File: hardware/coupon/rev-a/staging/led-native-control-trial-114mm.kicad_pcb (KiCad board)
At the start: 6 copper layers, 114 x 32.5 mm, 483 parts, among them J1 USB4505-03-0-A, J2 S2B-PH-SM4-TB, SW1 EVQP7J01P, SW2 JS202011JCQN, U1 TLC59581RTQT, U11 SN74LVC1G04DBVR, U17 SN74LVC1G11DBVR, U2 74HC4514PW,118, U23 SN74LVC1G06DBVR, U24 SN74LVC2G17DBVR, U25 SN74LVC2G17DBVR, U29 TPS70933DBVR, U3 ESP32-S3-WROOM-1U-N16R8, U31 TUSB320LAIRWBR, U32 TS3USB31ERSER, U33 TPD4E05U06DQAR, U34 TPS3808G01DBVR, U35 MAX17048G+T10, U36 TPS631000DRLR, U37 TPS63020DSJT, U38 2.5V shunt, U39 TMP390A2DRLR, U40 SN74AUP1G125DBVR, U41 BQ24074RGTR, U42 SN74AUP1G125DBVR, U43 SN74AUP1G125DBVR, U44 TPS259474ARPWR, U45 TPS259474ARPWR, U46 TCA9517ADGKR, U47 TPS3823A-33DBVR, U48 SN74LVC1G04DSFR, U49 SN74LVC1G74RSER, U50 SN74LVC1G74RSER, U51 SN74LVC1G11DRYR, U52 SN74LVC1G08DSFR, U53 TLV6700DSER, U54 SN74LVC2G00DCUR, U55 SN74LVC2G08DCUR

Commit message: Route application I2C data with an exact nearest-goal search
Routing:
- net SYS_I2C_SDA: track 37.6 -> 60.2 mm, vias 0 -> 4

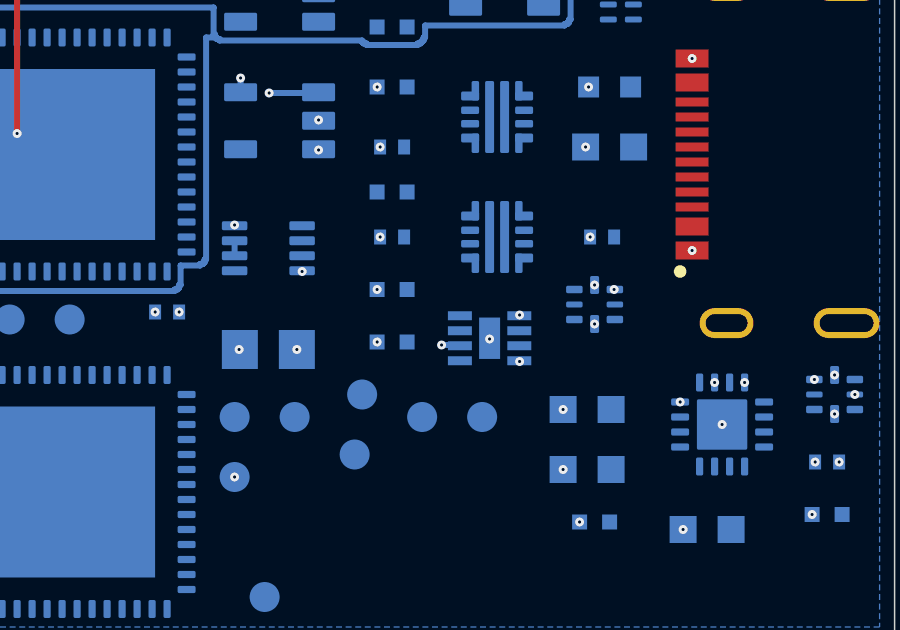
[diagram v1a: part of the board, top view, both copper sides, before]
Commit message: Complete gauge SDA with a supply-preserving layer detour
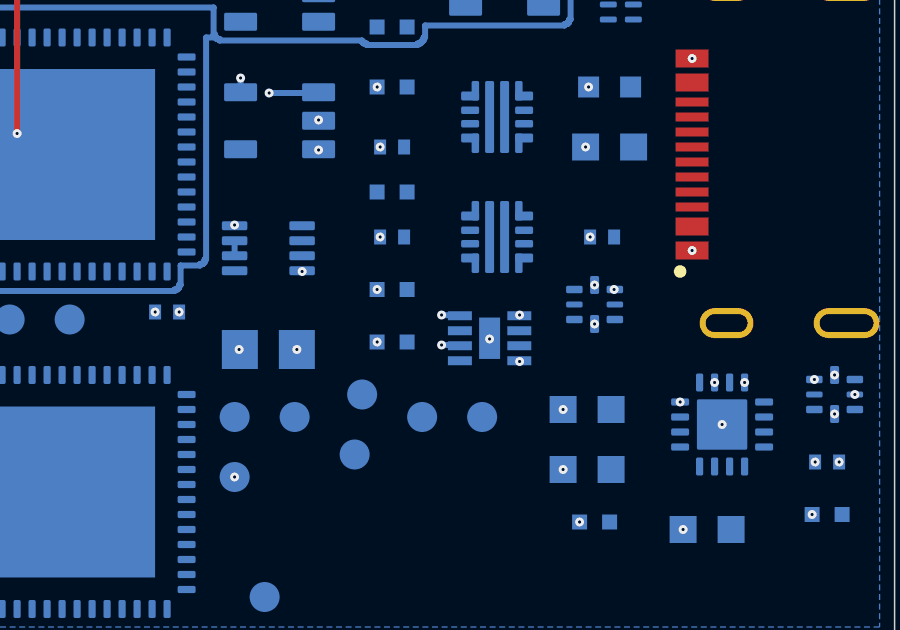
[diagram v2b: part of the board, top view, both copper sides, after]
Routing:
- net GAUGE_I2C_SDA: track 33.2 -> 112.4 mm, vias 4 -> 14
